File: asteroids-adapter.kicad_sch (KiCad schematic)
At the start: 16 parts, among them J1 Asteroids PCB connector, J2 Asteroids harness connector, U1 TL074

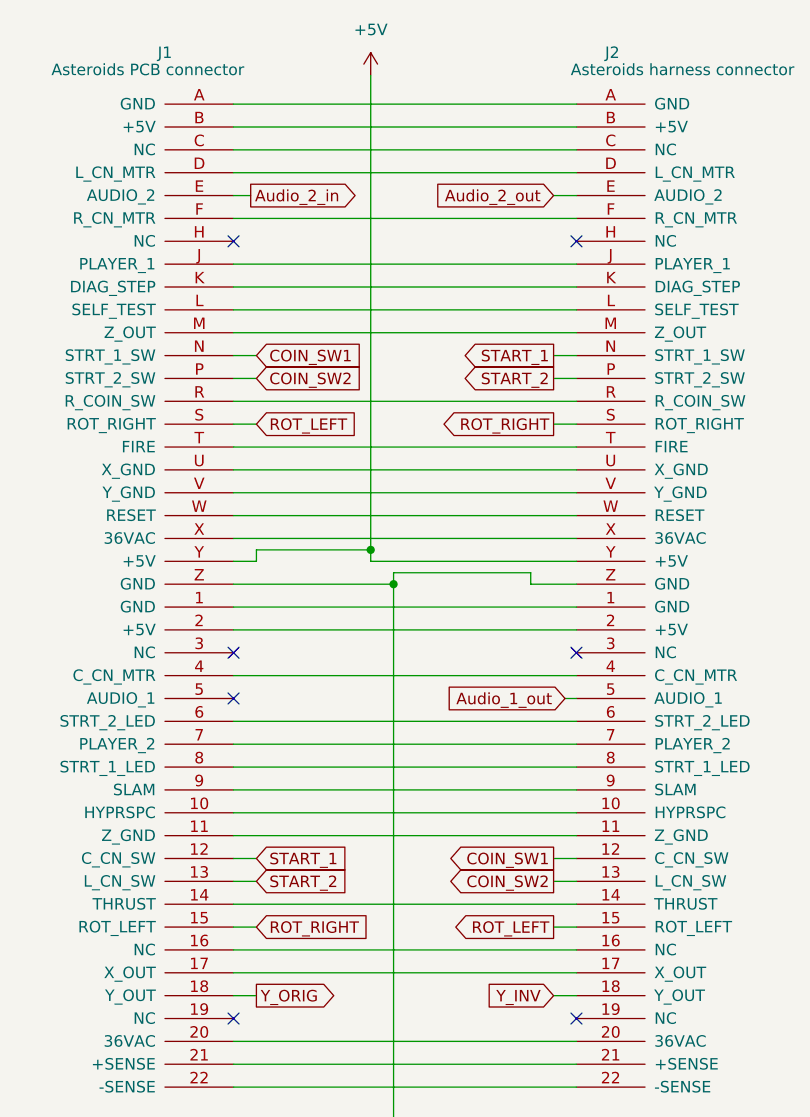
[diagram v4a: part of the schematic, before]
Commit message: Completed routing on compact PCB
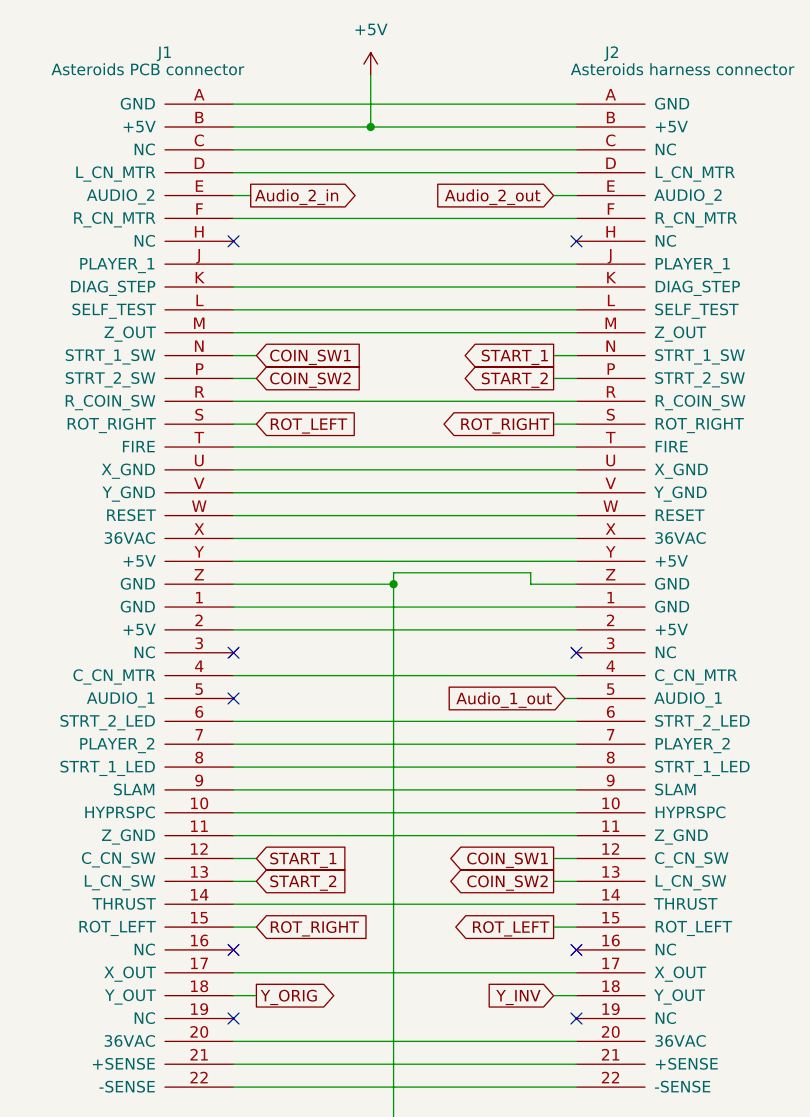
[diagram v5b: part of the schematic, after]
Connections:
- net +5V: now also J1.B (+5V), J2.B (+5V); no longer J1.Y (+5V), J2.Y (+5V)
- net at J2.16 (NC): no longer J1.16 (NC)
- new net: J1.Y (+5V), J2.Y (+5V)
- no-connect marks 7 -> 9
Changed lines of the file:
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@@
   (title_block
     (title "Asteroids to Asteroids Deluxe adapter")
-    (date "2022-02-24")
-    (rev "1.3")
-  )
-  (junction (at 62.23 72.39) (diameter 0) (color 0 0 0 0)
+    (date "2022-03-08")
+    (rev "1.4")
   )
   (junction (at 177.165 40.005) (diameter 0) (color 0 0 0 0)
@@
   )
   (junction (at 163.83 132.715) (diameter 0) (color 0 0 0 0)
+  )
+  (junction (at 62.23 25.4) (diameter 0) (color 0 0 0 0)
   )
   (junction (at 156.845 90.805) (diameter 0) (color 0 0 0 0)
@@
   (no_connect (at 46.99 83.82))
   (no_connect (at 46.99 38.1))
+  (no_connect (at 46.99 116.84))
   (no_connect (at 85.09 83.82))
+  (no_connect (at 85.09 116.84))
   (no_connect (at 46.99 88.9))
   (no_connect (at 85.09 38.1))
   (no_connect (at 85.09 124.46))
-  (wire (pts (xy 49.53 72.39) (xy 62.23 72.39))
-    (stroke (width 0) (type default) (color 0 0 0 0))
-  )
   (wire (pts (xy 46.99 30.48) (xy 85.09 30.48))
     (stroke (width 0) (type default) (color 0 0 0 0))
@@
     (stroke (width 0) (type default) (color 0 0 0 0))
   )
-  (wire (pts (xy 46.99 73.66) (xy 49.53 73.66))
-    (stroke (width 0) (type default) (color 0 0 0 0))
-  )
   (wire (pts (xy 172.72 124.46) (xy 163.83 124.46))
     (stroke (width 0) (type default) (color 0 0 0 0))
@@
     (stroke (width 0) (type default) (color 0 0 0 0))
   )
-  (wire (pts (xy 49.53 73.66) (xy 49.53 72.39))
-    (stroke (width 0) (type default) (color 0 0 0 0))
-  )
   (wire (pts (xy 46.99 76.2) (xy 64.77 76.2))
     (stroke (width 0) (type default) (color 0 0 0 0))
@@
     (stroke (width 0) (type default) (color 0 0 0 0))
   )
+  (wire (pts (xy 62.23 25.4) (xy 85.09 25.4))
+    (stroke (width 0) (type default) (color 0 0 0 0))
+  )
   (wire (pts (xy 163.195 95.885) (xy 160.02 95.885))
     (stroke (width 0) (type default) (color 0 0 0 0))
@@
     (stroke (width 0) (type default) (color 0 0 0 0))
   )
+  (wire (pts (xy 62.23 19.685) (xy 62.23 25.4))
+    (stroke (width 0) (type default) (color 0 0 0 0))
+  )
   (wire (pts (xy 191.77 124.46) (xy 180.34 124.46))
     (stroke (width 0) (type default) (color 0 0 0 0))
@@
     (stroke (width 0) (type default) (color 0 0 0 0))
   )
-  (wire (pts (xy 62.23 72.39) (xy 62.23 73.66))
-    (stroke (width 0) (type default) (color 0 0 0 0))
-  )
   (wire (pts (xy 169.545 29.845) (xy 169.545 41.275))
     (stroke (width 0) (type default) (color 0 0 0 0))
@@
     (stroke (width 0) (type default) (color 0 0 0 0))
   )
-  (wire (pts (xy 46.99 25.4) (xy 85.09 25.4))
+  (wire (pts (xy 46.99 25.4) (xy 62.23 25.4))
     (stroke (width 0) (type default) (color 0 0 0 0))
   )
@@
     (stroke (width 0) (type default) (color 0 0 0 0))
   )
-  (wire (pts (xy 62.23 19.685) (xy 62.23 72.39))
-    (stroke (width 0) (type default) (color 0 0 0 0))
-  )
   (wire (pts (xy 213.36 78.105) (xy 224.79 78.105))
     (stroke (width 0) (type default) (color 0 0 0 0))
@@
     (stroke (width 0) (type default) (color 0 0 0 0))
   )
-  (wire (pts (xy 46.99 116.84) (xy 85.09 116.84))
-    (stroke (width 0) (type default) (color 0 0 0 0))
-  )
   (wire (pts (xy 160.655 29.845) (xy 169.545 29.845))
     (stroke (width 0) (type default) (color 0 0 0 0))
@@
     (stroke (width 0) (type default) (color 0 0 0 0))
   )
-  (wire (pts (xy 62.23 73.66) (xy 85.09 73.66))
-    (stroke (width 0) (type default) (color 0 0 0 0))
-  )
+  (wire (pts (xy 46.99 73.66) (xy 85.09 73.66))
+    (stroke (width 0) (type default) (color 0 0 0 0))
+  )

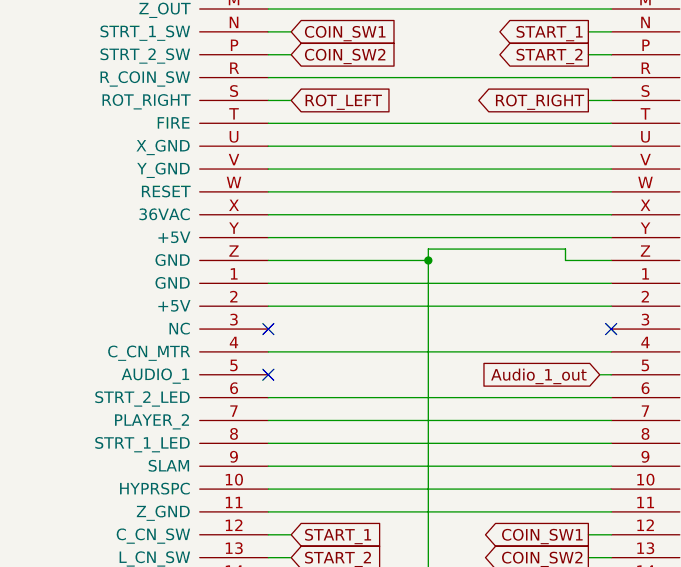
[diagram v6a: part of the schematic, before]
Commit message: Swith to PCB-mount edge connector
This is easier to assemble and provides a more reliable connection, due
to reduced likelyhood of distorting the edge connector position.
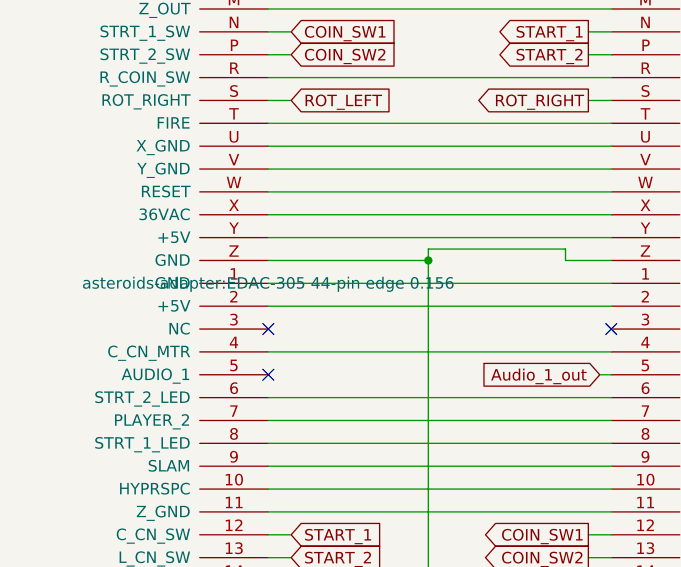
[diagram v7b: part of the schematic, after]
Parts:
- J1: footprint asteroids-adapter:edge 44-pin 0.156 inch -> asteroids-adapter:EDAC-305 44-pin edge 0.156
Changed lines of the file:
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@@
     (property "Reference" "J1" (id 0) (at 39.37 17.145 0))
     (property "Value" "Asteroids PCB connector" (id 1) (at 37.465 19.05 0))
-    (property "Footprint" "asteroids-adapter:edge 44-pin 0.156 inch" (id 2) (at 46.99 78.74 0)
-      (effects (font (size 1.27 1.27)) hide)
-    )
+    (property "Footprint" "asteroids-adapter:EDAC-305 44-pin edge 0.156" (id 2) (at 46.99 78.74 0))
     (property "Datasheet" "" (id 3) (at 46.99 78.74 0)
       (effects (font (size 1.27 1.27)) hide)
@@
     )
     (path "/c37cb6c3-6fec-4395-b191-aee0441c0811"
-      (reference "J1") (unit 1) (value "Asteroids PCB connector") (footprint "asteroids-adapter:edge 44-pin 0.156 inch")
+      (reference "J1") (unit 1) (value "Asteroids PCB connector") (footprint "asteroids-adapter:EDAC-305 44-pin edge 0.156")
     )
     (path "/a5880c02-3376-4fc6-b608-c3353c15c4ae"

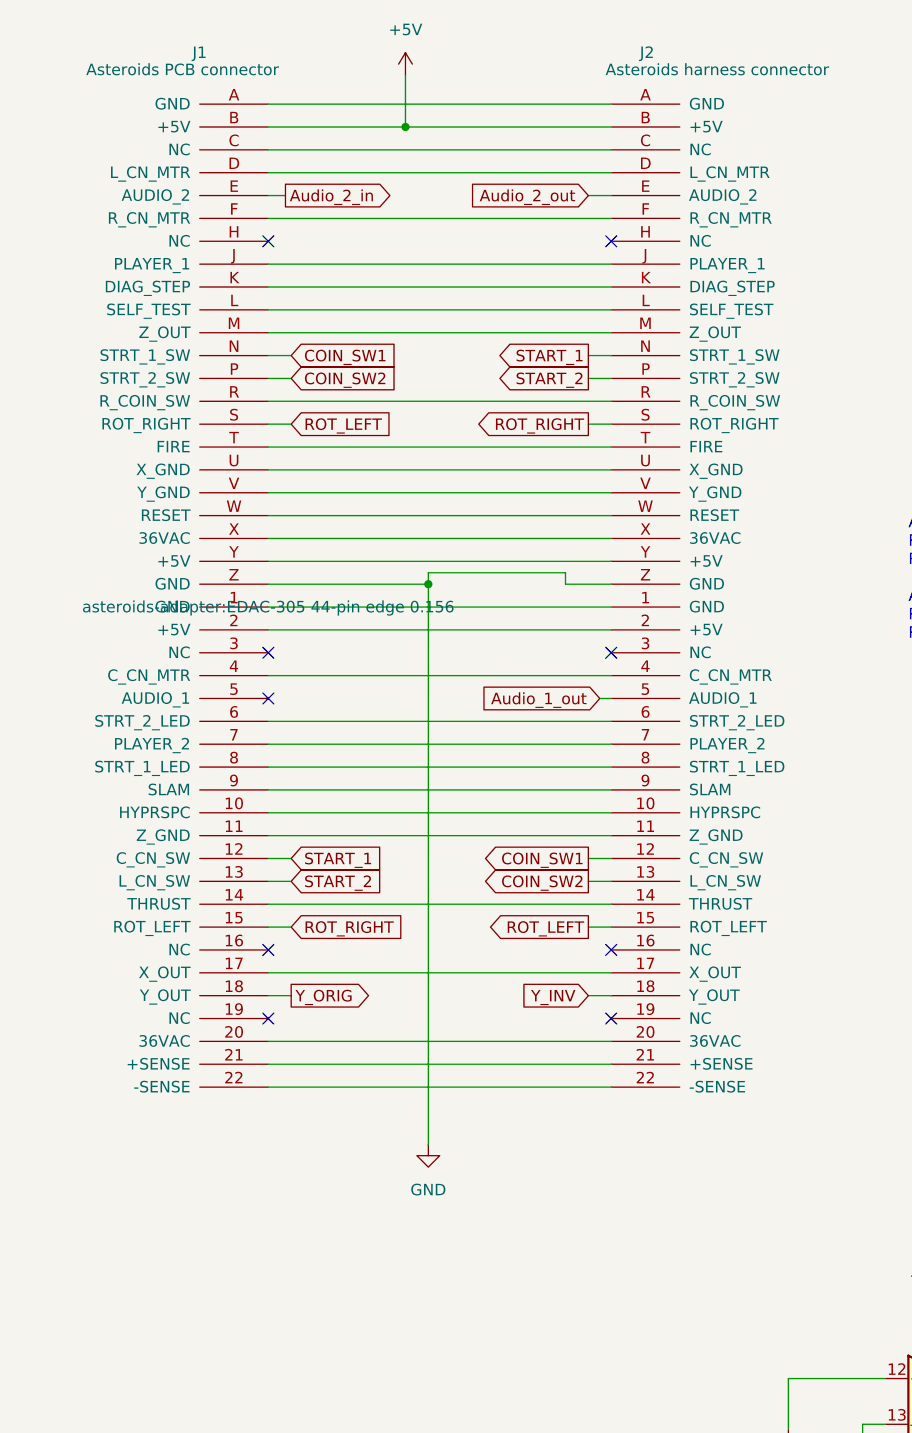
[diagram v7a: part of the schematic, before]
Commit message: Added connections for X_INV and Y_INV
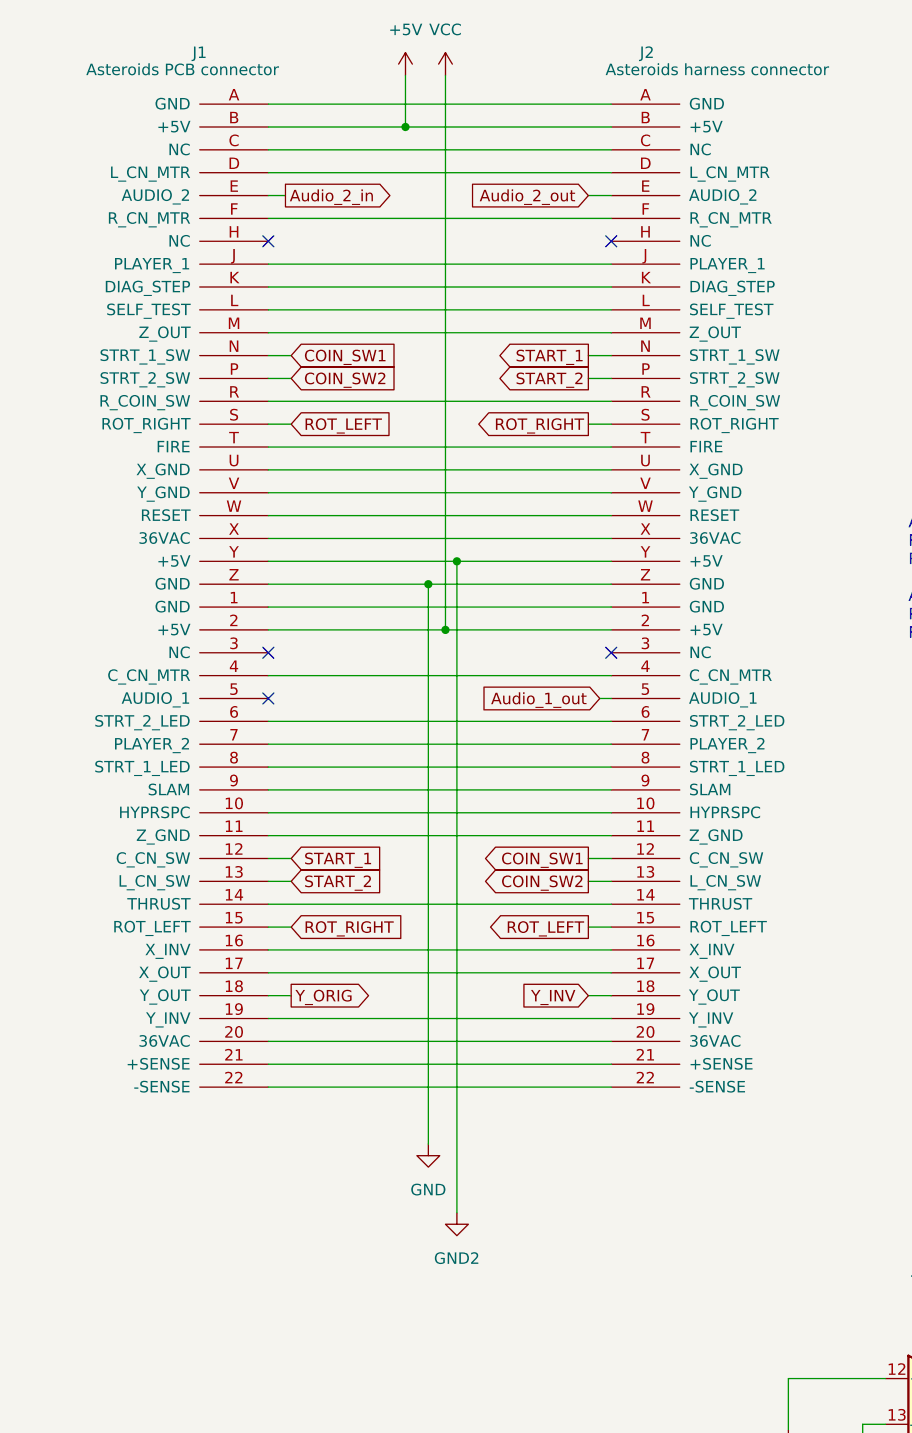
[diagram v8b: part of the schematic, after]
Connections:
- net at J2.16 (X_INV): now also J1.16 (X_INV)
- net at J2.19 (Y_INV): now also J1.19 (Y_INV)
- net VCC: now reaches J1.2 (+5V), J2.2 (+5V)
- net GND2: now reaches J1.Y (+5V), J2.Y (+5V)
- no-connect marks 9 -> 5
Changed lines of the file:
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@@
   (junction (at 184.785 93.345) (diameter 0) (color 0 0 0 0)
   )
+  (junction (at 66.675 81.28) (diameter 0) (color 0 0 0 0)
+  )
   (junction (at 182.88 93.345) (diameter 0) (color 0 0 0 0)
   )
@@
   (junction (at 163.83 132.715) (diameter 0) (color 0 0 0 0)
   )
+  (junction (at 67.945 73.66) (diameter 0) (color 0 0 0 0)
+  )
   (junction (at 62.23 25.4) (diameter 0) (color 0 0 0 0)
   )
@@
   (junction (at 163.195 50.165) (diameter 0) (color 0 0 0 0)
   )
-  (no_connect (at 46.99 124.46))
   (no_connect (at 46.99 83.82))
   (no_connect (at 46.99 38.1))
-  (no_connect (at 46.99 116.84))
   (no_connect (at 85.09 83.82))
-  (no_connect (at 85.09 116.84))
   (no_connect (at 46.99 88.9))
   (no_connect (at 85.09 38.1))
-  (no_connect (at 85.09 124.46))
   (wire (pts (xy 46.99 30.48) (xy 85.09 30.48))
     (stroke (width 0) (type default) (color 0 0 0 0))
@@
     (stroke (width 0) (type default) (color 0 0 0 0))
   )
-  (wire (pts (xy 64.77 74.93) (xy 80.01 74.93))
+  (wire (pts (xy 64.77 76.2) (xy 85.09 76.2))
     (stroke (width 0) (type default) (color 0 0 0 0))
   )
@@
     (stroke (width 0) (type default) (color 0 0 0 0))
   )
+  (wire (pts (xy 67.945 73.66) (xy 85.09 73.66))
+    (stroke (width 0) (type default) (color 0 0 0 0))
+  )
   (wire (pts (xy 82.55 114.3) (xy 85.09 114.3))
     (stroke (width 0) (type default) (color 0 0 0 0))
   )
-  (wire (pts (xy 80.01 76.2) (xy 85.09 76.2))
-    (stroke (width 0) (type default) (color 0 0 0 0))
-  )
   (wire (pts (xy 46.99 99.06) (xy 85.09 99.06))
     (stroke (width 0) (type default) (color 0 0 0 0))
@@
     (stroke (width 0) (type default) (color 0 0 0 0))
   )
-  (wire (pts (xy 64.77 74.93) (xy 64.77 76.2))
-    (stroke (width 0) (type default) (color 0 0 0 0))
-  )
   (wire (pts (xy 142.875 34.925) (xy 139.065 34.925))
     (stroke (width 0) (type default) (color 0 0 0 0))
@@
     (stroke (width 0) (type default) (color 0 0 0 0))
   )
-  (wire (pts (xy 80.01 74.93) (xy 80.01 76.2))
-    (stroke (width 0) (type default) (color 0 0 0 0))
-  )
   (wire (pts (xy 160.02 94.615) (xy 160.02 95.885))
     (stroke (width 0) (type default) (color 0 0 0 0))
@@
     (stroke (width 0) (type default) (color 0 0 0 0))
   )
+  (wire (pts (xy 46.99 124.46) (xy 85.09 124.46))
+    (stroke (width 0) (type default) (color 0 0 0 0))
+  )
+  (wire (pts (xy 67.945 73.66) (xy 67.945 146.05))
+    (stroke (width 0) (type default) (color 0 0 0 0))
+  )
+  (wire (pts (xy 66.675 81.28) (xy 85.09 81.28))
+    (stroke (width 0) (type default) (color 0 0 0 0))
+  )
   (wire (pts (xy 135.89 184.785) (xy 135.89 167.005))
     (stroke (width 0) (type default) (color 0 0 0 0))
@@
     (stroke (width 0) (type default) (color 0 0 0 0))
   )
+  (wire (pts (xy 66.675 19.685) (xy 66.675 81.28))
+    (stroke (width 0) (type default) (color 0 0 0 0))
+  )
   (wire (pts (xy 46.99 78.74) (xy 85.09 78.74))
     (stroke (width 0) (type default) (color 0 0 0 0))
@@
     (stroke (width 0) (type default) (color 0 0 0 0))
   )
-  (wire (pts (xy 46.99 81.28) (xy 85.09 81.28))
+  (wire (pts (xy 46.99 81.28) (xy 66.675 81.28))
     (stroke (width 0) (type default) (color 0 0 0 0))
   )
@@
     (stroke (width 0) (type default) (color 0 0 0 0))
   )
+  (wire (pts (xy 46.99 73.66) (xy 67.945 73.66))
+    (stroke (width 0) (type default) (color 0 0 0 0))
+  )
   (wire (pts (xy 46.99 58.42) (xy 49.53 58.42))
     (stroke (width 0) (type default) (color 0 0 0 0))
@@
     (stroke (width 0) (type default) (color 0 0 0 0))
   )
-  (wire (pts (xy 46.99 73.66) (xy 85.09 73.66))
-    (stroke (width 0) (type default) (color 0 0 0 0))
-  )
   (wire (pts (xy 163.83 124.46) (xy 163.83 132.715))
+    (stroke (width 0) (type default) (color 0 0 0 0))
+  )
+  (wire (pts (xy 46.99 116.84) (xy 85.09 116.84))
     (stroke (width 0) (type default) (color 0 0 0 0))
   )
@@
     (pin "2")
   )
+  (symbol (lib_id "power:VCC") (at 66.675 19.685 0) (unit 1)
+    (in_bom yes) (on_board yes) (fields_autoplaced)
+    (property "Reference" "#PWR?" (id 0) (at 66.675 23.495 0)
+      (effects (font (size 1.27 1.27)) hide)
+    )
+    (property "Value" "VCC" (id 1) (at 66.675 14.605 0))
+    (property "Footprint" "" (id 2) (at 66.675 19.685 0)
+      (effects (font (size 1.27 1.27)) hide)
+    )
+    (property "Datasheet" "" (id 3) (at 66.675 19.685 0)
+      (effects (font (size 1.27 1.27)) hide)
+    )
+    (pin "1")
+  )
   (symbol (lib_id "Amplifier_Operational:TL074") (at 123.19 167.005 0) (unit 5)
     (in_bom yes) (on_board yes)
@@
     (pin "1")
     (pin "2")
+  )
+  (symbol (lib_id "power:GND2") (at 67.945 146.05 0) (unit 1)
+    (in_bom yes) (on_board yes) (fields_autoplaced)
+    (property "Reference" "#PWR?" (id 0) (at 67.945 152.4 0)
+      (effects (font (size 1.27 1.27)) hide)
+    )
+    (property "Value" "GND2" (id 1) (at 67.945 151.13 0))
+    (property "Footprint" "" (id 2) (at 67.945 146.05 0)
+      (effects (font (size 1.27 1.27)) hide)
+    )
+    (property "Datasheet" "" (id 3) (at 67.945 146.05 0)
+      (effects (font (size 1.27 1.27)) hide)
+    )
+    (pin "1")
   )
   (symbol (lib_id "ast-adapter: Kemet MLCC 100 pF 5% 25V TH") (at 170.815 76.2 0) (unit 1)
@@
     (pin "2")
   )
-  (symbol (lib_id "ast-adapter:Asteroids I{slash}O connector") (at 46.99 78.74 0) (unit 1)
+  (symbol (lib_name "Asteroids I{slash}O connector_1") (lib_id "ast-adapter:Asteroids I{slash}O connector") (at 46.99 78.74 0) (unit 1)
     (in_bom yes) (on_board yes)
     (property "Reference" "J1" (id 0) (at 39.37 17.145 0))
     (property "Value" "Asteroids PCB connector" (id 1) (at 37.465 19.05 0))
-    (property "Footprint" "asteroids-adapter:EDAC-305 44-pin edge 0.156" (id 2) (at 46.99 78.74 0))
+    (property "Footprint" "asteroids-adapter:EDAC-305 44-pin edge 0.156" (id 2) (at 46.99 78.74 0)
+      (effects (font (size 1.27 1.27)) hide)
+    )
     (property "Datasheet" "" (id 3) (at 46.99 78.74 0)
       (effects (font (size 1.27 1.27)) hide)
@@
       (reference "#PWR0112") (unit 1) (value "GND") (footprint "")
     )
+    (path "/3a9f8db9-02b2-4d2e-b894-2cdea8761181"
+      (reference "#PWR?") (unit 1) (value "VCC") (footprint "")
+    )
+    (path "/53548fb5-eb77-4bd8-a617-81a0bcceb32e"
+      (reference "#PWR?") (unit 1) (value "GND2") (footprint "")
+    )
     (path "/b69dd169-bf84-4046-9a1b-6643baa5defd"
